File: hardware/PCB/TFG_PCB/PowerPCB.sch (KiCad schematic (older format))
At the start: 53 parts, among them J1 Conn_01x02_Male, J10 Conn_01x02_Male, J11 Conn_01x02_Male, J12 Conn_01x02_Male, J13 Conn_01x04_Male, J14 Conn_01x04_Male, J15 Conn_01x04_Male, J16 Conn_01x02_Male, J17 Conn_01x02_Male, J2 Conn_01x04_Male, J3 Conn_01x04_Male, J4 Conn_01x02_Male, J5 Conn_01x04_Male, J6 Conn_01x02_Male, J7 Conn_01x02_Male, J8 Conn_01x04_Male, J9 Conn_01x02_Male, Q1 IRF540N, Q2 FDD6685, Q3 FDD6685, Q4 2N7002, U1 L78L05_SOT89, U2 TD7590_2, U3 TD7590_2

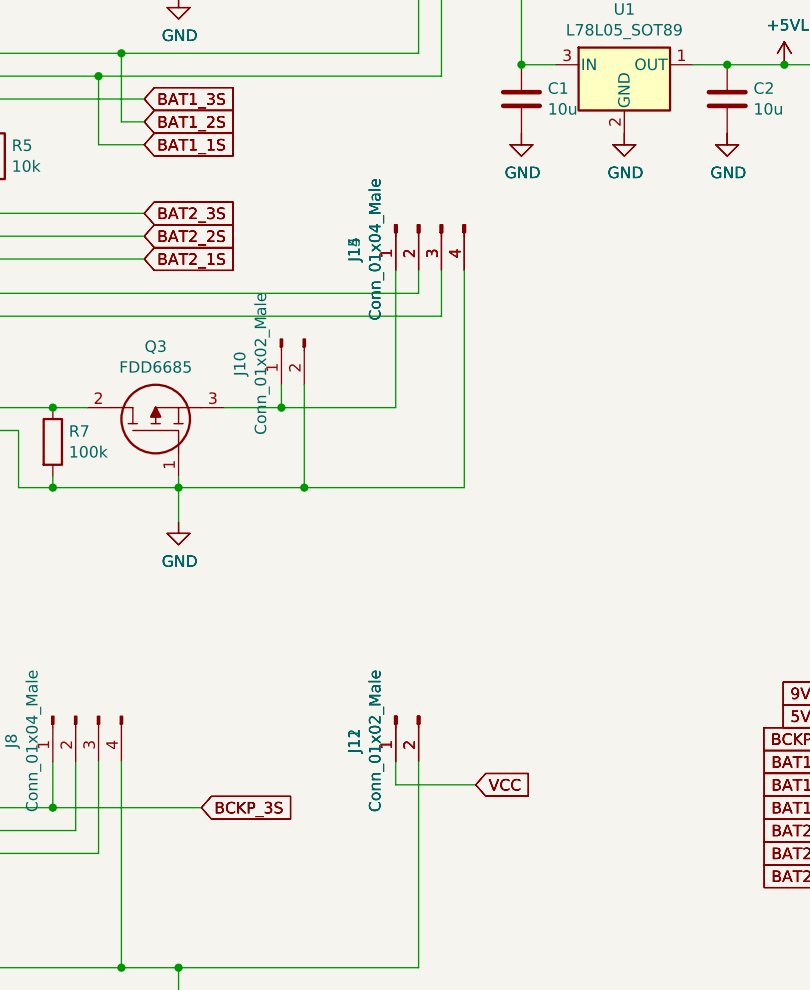
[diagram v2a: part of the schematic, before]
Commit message: Updated netlist and footprints
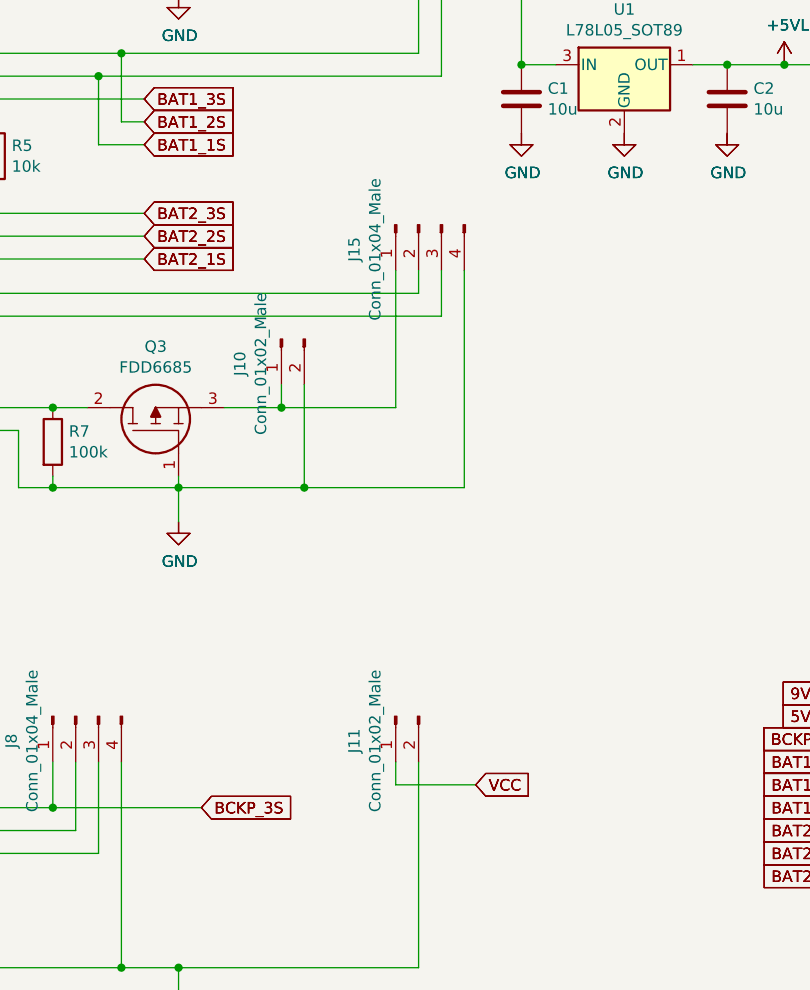
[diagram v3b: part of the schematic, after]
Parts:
- removed J12: Conn_01x02_Male, symbol Connector:Conn_01x02_Male
- removed J14: Conn_01x04_Male, symbol Connector:Conn_01x04_Male
- J1, J10, J11, J16, J17, J4, J6, J7, J9: footprint (none) -> Connector_Wire:SolderWirePad_1x02_P7.62mm_Drill2mm
- R1, R10, R11, R12, R13, R14, R15, R2, R3, R4, R5, R6, R7, R8, R9: footprint (none) -> Resistor_SMD:R_0805_2012Metric_Pad1.15x1.40mm_HandSolder
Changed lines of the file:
@@
 $Descr A4 11693 8268
 encoding utf-8
-Sheet 2 3
+Sheet 2 4
 Title "Power buses generation and control"
 Date "2020-01-24"
@@
 F 0 "J11" H 5258 5731 50  0000 C CNN
 F 1 "Conn_01x02_Male" H 5258 5640 50  0000 C CNN
-F 2 "" H 5150 5550 50  0001 C CNN
+F 2 "Connector_Wire:SolderWirePad_1x02_P7.62mm_Drill2mm" H 5150 5550 50  0001 C CNN
 F 3 "~" H 5150 5550 50  0001 C CNN
 	1    5150 5550
@@
 Wire Wire Line
 	3650 4550 4200 4550
-$Comp
-L Connector:Conn_01x04_Male J?
-U 1 1 5E76290B
-P 5250 3400
-AR Path="/5E76290B" Ref="J?"  Part="1"
-AR Path="/5E6BD4F2/5E76290B" Ref="J14"  Part="1"
-F 0 "J14" H 5358 3681 50  0000 C CNN
-F 1 "Conn_01x04_Male" H 5358 3590 50  0000 C CNN
-F 2 "" H 5250 3400 50  0001 C CNN
-F 3 "~" H 5250 3400 50  0001 C CNN
-	1    5250 3400
-	0    -1   1    0
-$EndComp
 Wire Wire Line
 	5150 1800 5150 1900
@@
 F 0 "J6" H 1808 6731 50  0000 C CNN
 F 1 "Conn_01x02_Male" H 1808 6640 50  0000 C CNN
-F 2 "" H 1700 6550 50  0001 C CNN
+F 2 "Connector_Wire:SolderWirePad_1x02_P7.62mm_Drill2mm" H 1700 6550 50  0001 C CNN
 F 3 "~" H 1700 6550 50  0001 C CNN
 	1    1700 6550
@@
 F 0 "J7" H 3258 5731 50  0000 C CNN
 F 1 "Conn_01x02_Male" H 3258 5640 50  0000 C CNN
-F 2 "" H 3150 5550 50  0001 C CNN
+F 2 "Connector_Wire:SolderWirePad_1x02_P7.62mm_Drill2mm" H 3150 5550 50  0001 C CNN
 F 3 "~" H 3150 5550 50  0001 C CNN
 	1    3150 5550
@@
 F 0 "R2" H 2420 6846 50  0000 L CNN
 F 1 "10k" H 2420 6755 50  0000 L CNN
-F 2 "" V 2280 6800 50  0001 C CNN
+F 2 "Resistor_SMD:R_0805_2012Metric_Pad1.15x1.40mm_HandSolder" V 2280 6800 50  0001 C CNN
 F 3 "~" H 2350 6800 50  0001 C CNN
 	1    2350 6800
@@
 Text GLabel 4300 5950 2    50   Input ~ 0
 BCKP_3S
-$Comp
-L Connector:Conn_01x02_Male J?
-U 1 1 5E97A704
-P 5150 5550
-AR Path="/5E97A704" Ref="J?"  Part="1"
-AR Path="/5E6BD4F2/5E97A704" Ref="J12"  Part="1"
-F 0 "J12" H 5258 5731 50  0000 C CNN
-F 1 "Conn_01x02_Male" H 5258 5640 50  0000 C CNN
-F 2 "" H 5150 5550 50  0001 C CNN
-F 3 "~" H 5150 5550 50  0001 C CNN
-	1    5150 5550
-	0    -1   1    0
-$EndComp
 Text GLabel 5500 5850 2    50   Input ~ 0
 VCC
@@
 F 0 "J1" H 1808 2081 50  0000 C CNN
 F 1 "Conn_01x02_Male" H 1808 1990 50  0000 C CNN
-F 2 "" H 1700 1900 50  0001 C CNN
+F 2 "Connector_Wire:SolderWirePad_1x02_P7.62mm_Drill2mm" H 1700 1900 50  0001 C CNN
 F 3 "~" H 1700 1900 50  0001 C CNN
 	1    1700 1900
@@
 F 0 "J4" H 1808 4381 50  0000 C CNN
 F 1 "Conn_01x02_Male" H 1808 4290 50  0000 C CNN
-F 2 "" H 1700 4200 50  0001 C CNN
+F 2 "Connector_Wire:SolderWirePad_1x02_P7.62mm_Drill2mm" H 1700 4200 50  0001 C CNN
 F 3 "~" H 1700 4200 50  0001 C CNN
 	1    1700 4200
@@
 F 0 "R5" H 3470 3146 50  0000 L CNN
 F 1 "10k" H 3470 3055 50  0000 L CNN
-F 2 "" V 3330 3100 50  0001 C CNN
+F 2 "Resistor_SMD:R_0805_2012Metric_Pad1.15x1.40mm_HandSolder" V 3330 3100 50  0001 C CNN
 F 3 "~" H 3400 3100 50  0001 C CNN
 	1    3400 3100
@@
 F 0 "R3" H 2920 3146 50  0000 L CNN
 F 1 "10k" H 2920 3055 50  0000 L CNN
-F 2 "" V 2780 3100 50  0001 C CNN
+F 2 "Resistor_SMD:R_0805_2012Metric_Pad1.15x1.40mm_HandSolder" V 2780 3100 50  0001 C CNN
 F 3 "~" H 2850 3100 50  0001 C CNN
 	1    2850 3100
@@
 F 0 "R4" H 3170 3146 50  0000 L CNN
 F 1 "10k" H 3170 3055 50  0000 L CNN
-F 2 "" V 3030 3100 50  0001 C CNN
+F 2 "Resistor_SMD:R_0805_2012Metric_Pad1.15x1.40mm_HandSolder" V 3030 3100 50  0001 C CNN
 F 3 "~" H 3100 3100 50  0001 C CNN
 	1    3100 3100
@@
 F 0 "R6" H 3720 2096 50  0000 L CNN
 F 1 "100k" H 3720 2005 50  0000 L CNN
-F 2 "" V 3580 2050 50  0001 C CNN
+F 2 "Resistor_SMD:R_0805_2012Metric_Pad1.15x1.40mm_HandSolder" V 3580 2050 50  0001 C CNN
 F 3 "~" H 3650 2050 50  0001 C CNN
 	1    3650 2050
@@
 F 0 "R7" H 3720 4396 50  0000 L CNN
 F 1 "100k" H 3720 4305 50  0000 L CNN
-F 2 "" V 3580 4350 50  0001 C CNN
+F 2 "Resistor_SMD:R_0805_2012Metric_Pad1.15x1.40mm_HandSolder" V 3580 4350 50  0001 C CNN
 F 3 "~" H 3650 4350 50  0001 C CNN
 	1    3650 4350
@@
 F 0 "J9" H 4758 1781 50  0000 C CNN
 F 1 "Conn_01x02_Male" H 4758 1690 50  0000 C CNN
-F 2 "" H 4650 1600 50  0001 C CNN
+F 2 "Connector_Wire:SolderWirePad_1x02_P7.62mm_Drill2mm" H 4650 1600 50  0001 C CNN
 F 3 "~" H 4650 1600 50  0001 C CNN
 	1    4650 1600
@@
 F 0 "J10" H 4758 4081 50  0000 C CNN
 F 1 "Conn_01x02_Male" H 4758 3990 50  0000 C CNN
-F 2 "" H 4650 3900 50  0001 C CNN
+F 2 "Connector_Wire:SolderWirePad_1x02_P7.62mm_Drill2mm" H 4650 3900 50  0001 C CNN
 F 3 "~" H 4650 3900 50  0001 C CNN
 	1    4650 3900
@@
 F 0 "J16" H 6308 1781 50  0000 C CNN
 F 1 "Conn_01x02_Male" H 6308 1690 50  0000 C CNN
-F 2 "" H 6200 1600 50  0001 C CNN
+F 2 "Connector_Wire:SolderWirePad_1x02_P7.62mm_Drill2mm" H 6200 1600 50  0001 C CNN
 F 3 "~" H 6200 1600 50  0001 C CNN
 	1    6200 1600
@@
 F 0 "J17" H 6708 1781 50  0000 C CNN
 F 1 "Conn_01x02_Male" H 6708 1690 50  0000 C CNN
-F 2 "" H 6600 1600 50  0001 C CNN
+F 2 "Connector_Wire:SolderWirePad_1x02_P7.62mm_Drill2mm" H 6600 1600 50  0001 C CNN
 F 3 "~" H 6600 1600 50  0001 C CNN
 	1    6600 1600
@@
 F 0 "R10" H 9970 2196 50  0000 L CNN
 F 1 "300k" H 9970 2105 50  0000 L CNN
-F 2 "" V 9830 2150 50  0001 C CNN
+F 2 "Resistor_SMD:R_0805_2012Metric_Pad1.15x1.40mm_HandSolder" V 9830 2150 50  0001 C CNN
 F 3 "~" H 9900 2150 50  0001 C CNN
 	1    9900 2150
@@
 F 0 "R11" H 9970 4396 50  0000 L CNN
 F 1 "68k" H 9970 4305 50  0000 L CNN
-F 2 "" V 9830 4350 50  0001 C CNN
+F 2 "Resistor_SMD:R_0805_2012Metric_Pad1.15x1.40mm_HandSolder" V 9830 4350 50  0001 C CNN
 F 3 "~" H 9900 4350 50  0001 C CNN
 	1    9900 4350
@@
 F 0 "R12" V 9943 1900 50  0000 C CNN
 F 1 "47k" V 10034 1900 50  0000 C CNN
-F 2 "" V 10080 1900 50  0001 C CNN
+F 2 "Resistor_SMD:R_0805_2012Metric_Pad1.15x1.40mm_HandSolder" V 10080 1900 50  0001 C CNN
 F 3 "~" H 10150 1900 50  0001 C CNN
 	1    10150 1900
@@
 F 0 "R13" V 9943 4100 50  0000 C CNN
 F 1 "22k" V 10034 4100 50  0000 C CNN
-F 2 "" V 10080 4100 50  0001 C CNN
+F 2 "Resistor_SMD:R_0805_2012Metric_Pad1.15x1.40mm_HandSolder" V 10080 4100 50  0001 C CNN
 F 3 "~" H 10150 4100 50  0001 C CNN
 	1    10150 4100
@@
 F 0 "R9" H 8170 4546 50  0000 L CNN
 F 1 "10k" H 8170 4455 50  0000 L CNN
-F 2 "" V 8030 4500 50  0001 C CNN
+F 2 "Resistor_SMD:R_0805_2012Metric_Pad1.15x1.40mm_HandSolder" V 8030 4500 50  0001 C CNN
 F 3 "~" H 8100 4500 50  0001 C CNN
 	1    8100 4500
@@
 F 0 "R8" H 8170 2346 50  0000 L CNN
 F 1 "10k" H 8170 2255 50  0000 L CNN
-F 2 "" V 8030 2300 50  0001 C CNN
+F 2 "Resistor_SMD:R_0805_2012Metric_Pad1.15x1.40mm_HandSolder" V 8030 2300 50  0001 C CNN
 F 3 "~" H 8100 2300 50  0001 C CNN
 	1    8100 2300
@@
 F 0 "R14" H 8370 1446 50  0000 L CNN
 F 1 "10k" H 8370 1355 50  0000 L CNN
-F 2 "" V 8230 1400 50  0001 C CNN
+F 2 "Resistor_SMD:R_0805_2012Metric_Pad1.15x1.40mm_HandSolder" V 8230 1400 50  0001 C CNN
 F 3 "~" H 8300 1400 50  0001 C CNN
 	1    8300 1400
@@
 F 0 "R1" H 8370 1046 50  0000 L CNN
 F 1 "10k" H 8370 955 50  0000 L CNN
-F 2 "" V 8230 1000 50  0001 C CNN
+F 2 "Resistor_SMD:R_0805_2012Metric_Pad1.15x1.40mm_HandSolder" V 8230 1000 50  0001 C CNN
 F 3 "~" H 8300 1000 50  0001 C CNN
 	1    8300 1000
@@
 F 0 "R15" H 8420 3896 50  0000 L CNN
 F 1 "10k" H 8420 3805 50  0000 L CNN
-F 2 "" V 8280 3850 50  0001 C CNN
+F 2 "Resistor_SMD:R_0805_2012Metric_Pad1.15x1.40mm_HandSolder" V 8280 3850 50  0001 C CNN
 F 3 "~" H 8350 3850 50  0001 C CNN
 	1    8350 3850
